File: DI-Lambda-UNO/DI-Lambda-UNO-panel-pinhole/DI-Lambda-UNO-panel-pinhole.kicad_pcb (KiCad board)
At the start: 2 copper layers, 33.2 x 26.6 mm, 1 part

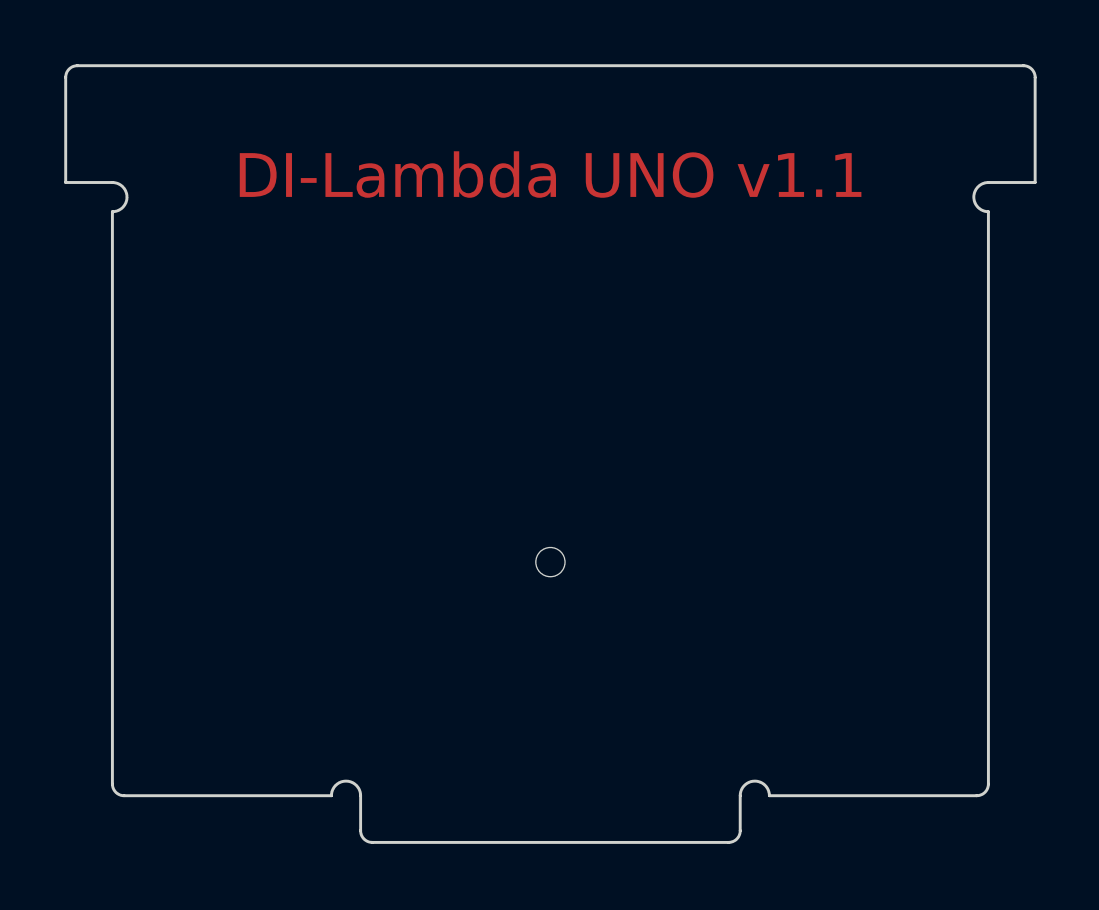
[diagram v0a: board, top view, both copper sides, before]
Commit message: Change pinhole tab length to 15mm
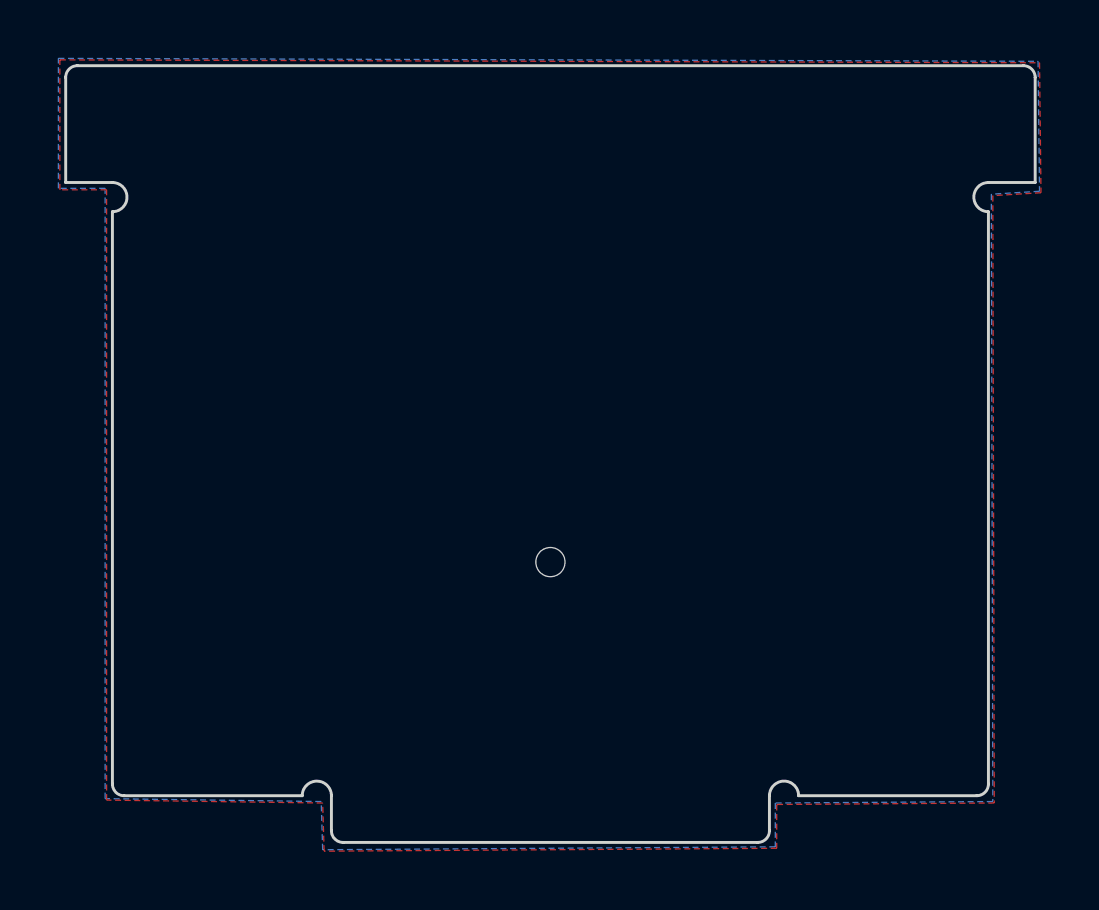
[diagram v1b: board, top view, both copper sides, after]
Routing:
- added copper zone on B.Cu, net (none)
- added copper zone on F.Cu, net (none)
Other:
- outline, holes or cut-outs redrawn
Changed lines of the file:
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@@
     (mod_text_size 1 1)
     (mod_text_width 0.15)
-    (pad_size 1.524 1.524)
-    (pad_drill 0.762)
+    (pad_size 1 1)
+    (pad_drill 1)
     (pad_to_mask_clearance 0.2)
     (aux_axis_origin 143.4 67)
@@
     (visible_elements FFFFFF7F)
     (pcbplotparams
-      (layerselection 0x000c0_7fffffff)
+      (layerselection 0x010f0_ffffffff)
       (usegerberextensions true)
       (usegerberattributes true)
@@
       (drillshape 0)
       (scaleselection 1)
-      (outputdirectory DI-Lambda-UNO-panel-pinhole-v1.0-gerbers-20170824/))
+      (outputdirectory DI-Lambda-UNO-panel-pinhole-v1.1-gerbers-2017oct25/))
   )
   (net 0 "")
@@
       (effects (font (size 1 1) (thickness 0.15)))
     )
-    (pad "" np_thru_hole circle (at 0 0) (size 1 1) (drill 1) (layers *.Cu *.Mask))
+    (pad "" np_thru_hole circle (at 0 0) (size 1 1) (drill 1) (layers *.Cu))
   )
-  (gr_text "DI-Lambda UNO v1.1" (at 160 70.8) (layer F.Cu)
+  (gr_text "DI-Lambda UNO v1.1" (at 160 70.8) (layer F.Mask)
     (effects (font (size 1.5 1.5) (thickness 0.3)))
   )
@@
   (gr_arc (start 174.6 91.6) (end 175 91.6) (angle 90) (layer Edge.Cuts) (width 0.1))
   (gr_arc (start 145.4 91.6) (end 145.4 92) (angle 90) (layer Edge.Cuts) (width 0.1))
-  (gr_arc (start 166.1 93.2) (end 166.5 93.2) (angle 90) (layer Edge.Cuts) (width 0.1))
-  (gr_arc (start 153.9 93.2) (end 153.9 93.6) (angle 90) (layer Edge.Cuts) (width 0.1))
-  (gr_arc (start 167 92) (end 166.5 92) (angle 180) (layer Edge.Cuts) (width 0.1))
-  (gr_arc (start 153 92) (end 152.5 92) (angle 180) (layer Edge.Cuts) (width 0.1))
+  (gr_arc (start 167.1 93.2) (end 167.5 93.2) (angle 90) (layer Edge.Cuts) (width 0.1))
+  (gr_arc (start 152.9 93.2) (end 152.9 93.6) (angle 90) (layer Edge.Cuts) (width 0.1))
+  (gr_arc (start 168 92) (end 167.5 92) (angle 180) (layer Edge.Cuts) (width 0.1))
+  (gr_arc (start 152 92) (end 151.5 92) (angle 180) (layer Edge.Cuts) (width 0.1))
   (gr_line (start 175 91.6) (end 175 72) (layer Edge.Cuts) (width 0.1))
   (gr_line (start 176.2 67) (end 143.8 67) (layer Edge.Cuts) (width 0.1))
   (gr_line (start 175 71) (end 176.6 71) (layer Edge.Cuts) (width 0.1))
   (gr_line (start 145 91.6) (end 145 72) (layer Edge.Cuts) (width 0.1))
-  (gr_line (start 174.6 92) (end 167.5 92) (layer Edge.Cuts) (width 0.1))
+  (gr_line (start 174.6 92) (end 168.5 92) (layer Edge.Cuts) (width 0.1))
   (gr_line (start 176.6 67.4) (end 176.6 71) (layer Edge.Cuts) (width 0.1))
-  (gr_line (start 166.5 93.2) (end 166.5 92) (layer Edge.Cuts) (width 0.1))
-  (gr_line (start 153.9 93.6) (end 166.1 93.6) (layer Edge.Cuts) (width 0.1))
+  (gr_line (start 167.5 93.2) (end 167.5 92) (layer Edge.Cuts) (width 0.1))
+  (gr_line (start 152.9 93.6) (end 167.1 93.6) (layer Edge.Cuts) (width 0.1))
   (gr_line (start 143.4 71) (end 143.4 67.4) (layer Edge.Cuts) (width 0.1))
   (gr_line (start 145 71) (end 143.4 71) (layer Edge.Cuts) (width 0.1))
-  (gr_line (start 153.5 92) (end 153.5 93.2) (layer Edge.Cuts) (width 0.1))
-  (gr_line (start 145.4 92) (end 152.5 92) (layer Edge.Cuts) (width 0.1))
+  (gr_line (start 152.5 92) (end 152.5 93.2) (layer Edge.Cuts) (width 0.1))
+  (gr_line (start 145.4 92) (end 151.5 92) (layer Edge.Cuts) (width 0.1))
+  (zone (net 0) (net_name "") (layer F.Cu) (hatch edge 0.508)
+    (connect_pads (clearance 0.508))
+    (min_thickness 0.254)
+    (fill yes (arc_segments 16) (thermal_gap 0.508) (thermal_bridge_width 0.508))
+    (polygon
+      (pts
+        (xy 143.2 66.8) (xy 176.75 66.9) (xy 176.8 71.35) (xy 175.15 71.45) (xy 175.2 92.25)
+        (xy 167.75 92.3) (xy 167.75 93.8) (xy 152.25 93.9) (xy 152.2 92.25) (xy 144.8 92.15)
+        (xy 144.8 71.25) (xy 143.2 71.25)
+      )
+    )
+  )
+  (zone (net 0) (net_name "") (layer B.Cu) (hatch edge 0.508)
+    (connect_pads (clearance 0.508))
+    (min_thickness 0.254)
+    (fill yes (arc_segments 16) (thermal_gap 0.508) (thermal_bridge_width 0.508))
+    (polygon
+      (pts
+        (xy 143.15 66.75) (xy 176.7 66.85) (xy 176.75 71.3) (xy 175.1 71.4) (xy 175.15 92.2)
+        (xy 167.7 92.25) (xy 167.7 93.75) (xy 152.2 93.85) (xy 152.15 92.2) (xy 144.75 92.1)
+        (xy 144.75 71.2) (xy 143.15 71.2)
+      )
+    )
+  )
 )
